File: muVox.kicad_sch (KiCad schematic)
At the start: 58 parts, among them J1 STEMMA QT, J2 Conn_01x06, J3 Alt.DC, J4 DC IN, J5 JTAG_EXTRA, SW1 EG120A, U1 TPS5430DDA, U2 XC6220B331MR, U3 ZD24C08AE1

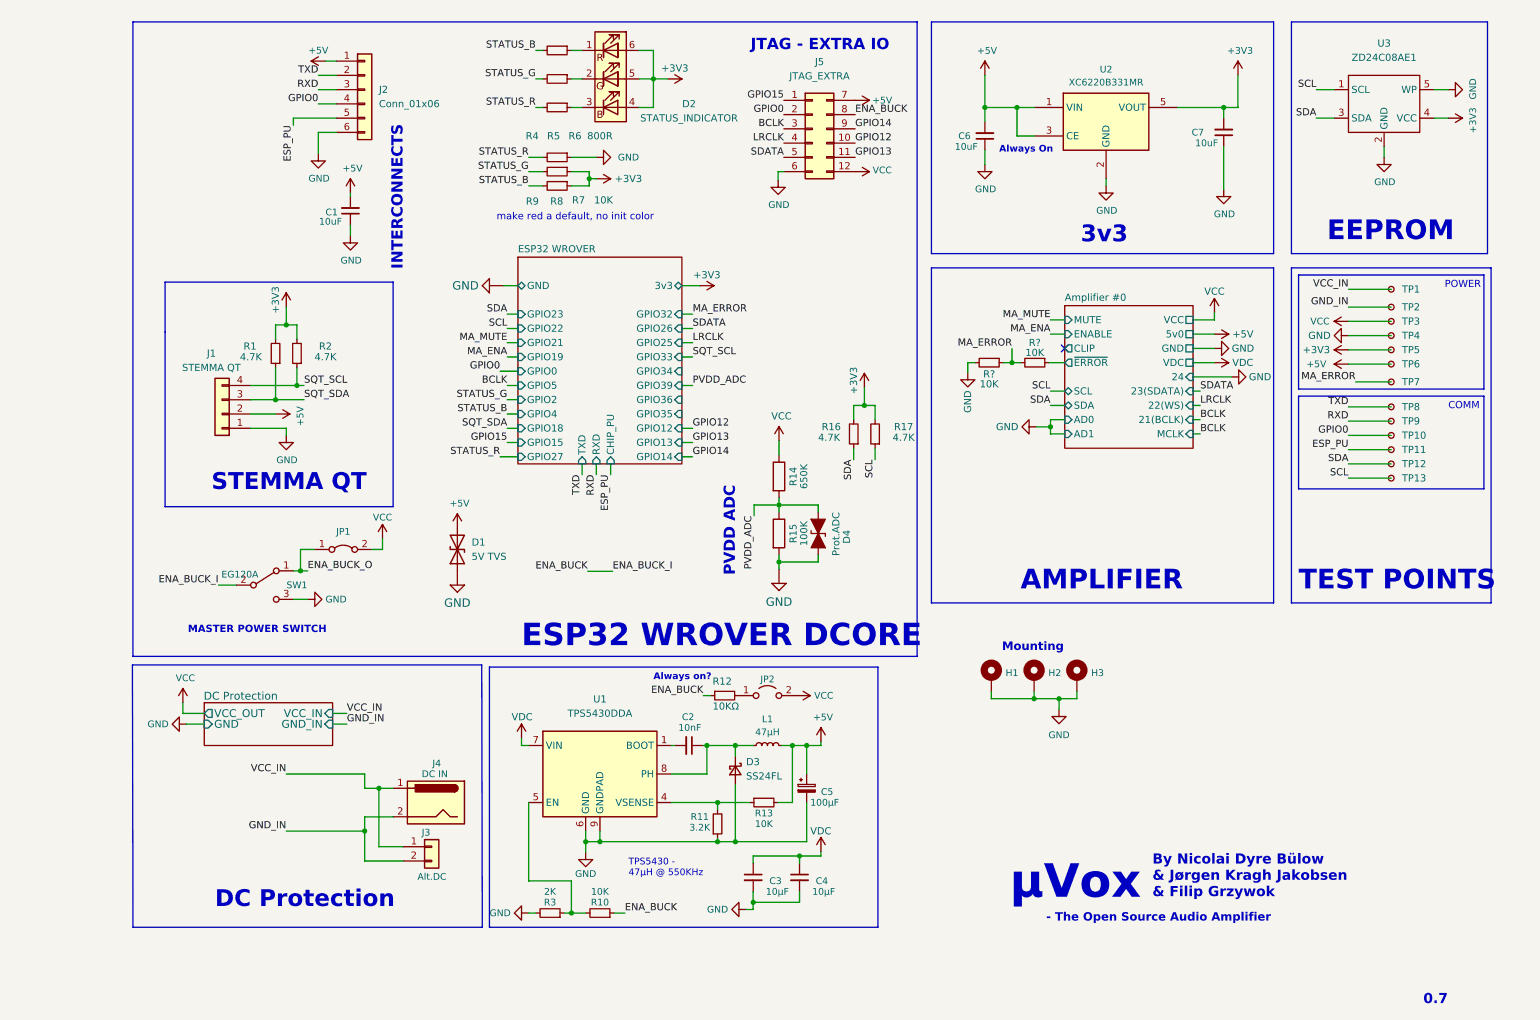
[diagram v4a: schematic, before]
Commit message: Lastest changes. Finetuned Filips routing and OCDd over the silkscreening.
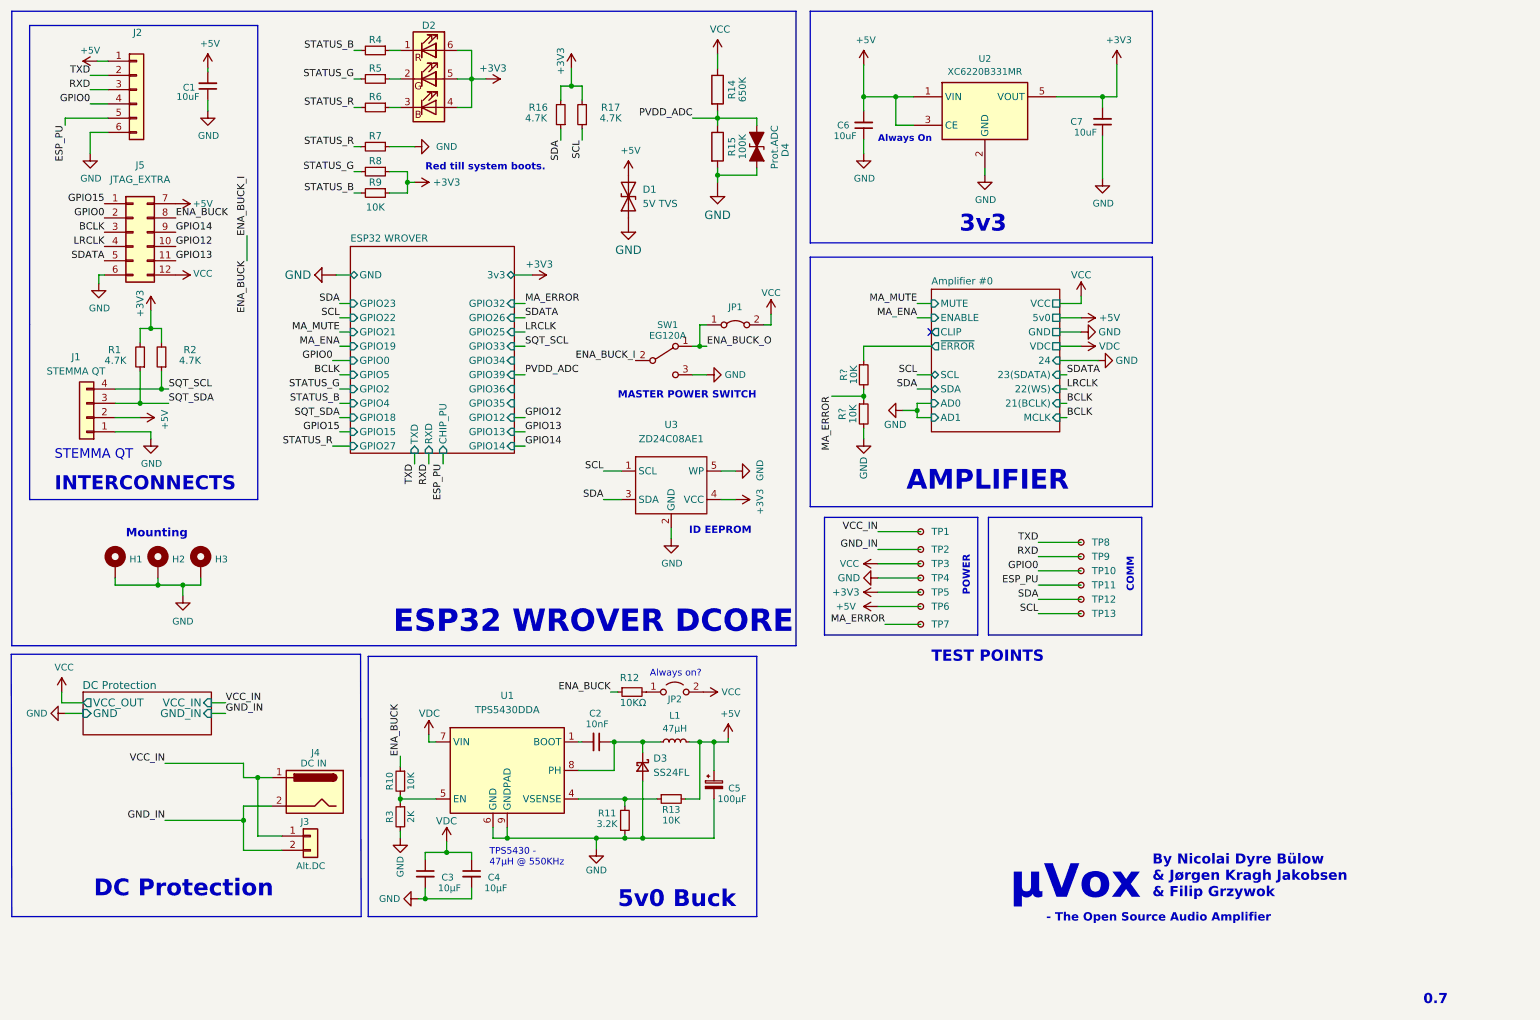
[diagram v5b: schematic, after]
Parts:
- D2: value STATUS_INDICATOR -> (none)
- J2: value Conn_01x06 -> (none)
- R6: value 800R -> (none)
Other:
- note added: "5v0 Buck"
- note added: "ID EEPROM"
- note added: "Red till system boots."
- note removed: "EEPROM"
- note removed: "JTAG - EXTRA IO"
- note removed: "PVDD ADC"
- note removed: "make red a default, no init color"
- moved on the sheet: C1, C2, C3, C4, C5, C6, C7, D1, D2, D3, D4, H1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

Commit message: Lastest revised files. Loads more DC protection now, thanks to @feelfreelinux
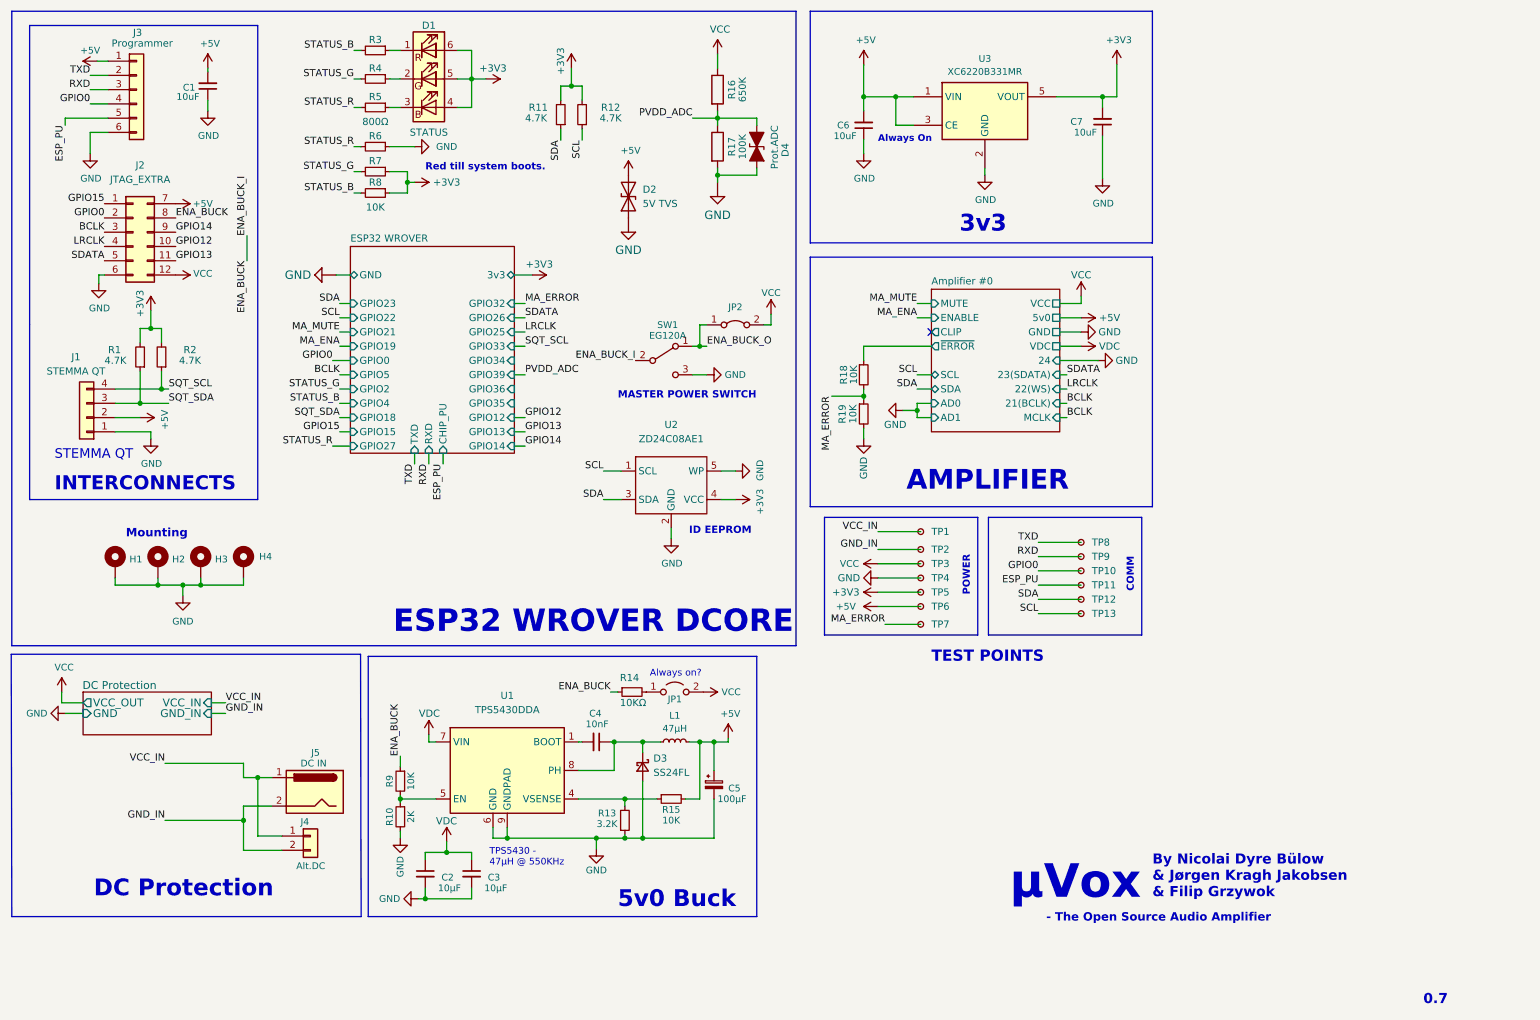
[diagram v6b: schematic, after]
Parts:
- added H4: MountingHole_Pad, Lib:MountingHole_PSUDO_M4, symbol Mechanical:MountingHole_Pad
- D1: renamed from D2; value (none) -> STATUS; Identifier 67-23/R6GHBHC-B05/2T -> FYLS-5050NRGBC
- H1, H2, H3: footprint MountingHole:MountingHole_3.2mm_M3_DIN965_Pad -> Lib:MountingHole_PSUDO_M4
- J3: renamed from J2; value (none) -> Programmer
- R5: renamed from R6; value (none) -> 800Ω
- gave numbers to parts that had none: 2
- renumbered C3 to C2, C4 to C3, C2 to C4, D1 to D2, J5 to J2, J3 to J4, J4 to J5, JP2 to JP1, JP1 to JP2, R3 to R10, R16 to R11, R17 to R12, R11 to R13, R12 to R14, R13 to R15, R14 to R16, R15 to R17, R4 to R3, R5 to R4, R7 to R6, R8 to R7, R9 to R8, R10 to R9, U3 to U2, U2 to U3
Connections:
- net GND: now also H4.1
